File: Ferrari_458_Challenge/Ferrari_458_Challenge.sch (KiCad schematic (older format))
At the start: 16 parts, among them P1 SERVO, P2 ESC, P3 LEFT_IR, P4 RIGHT_IR, P5 ULTRASONIC, U1 LM7805, U2 FS-R6B

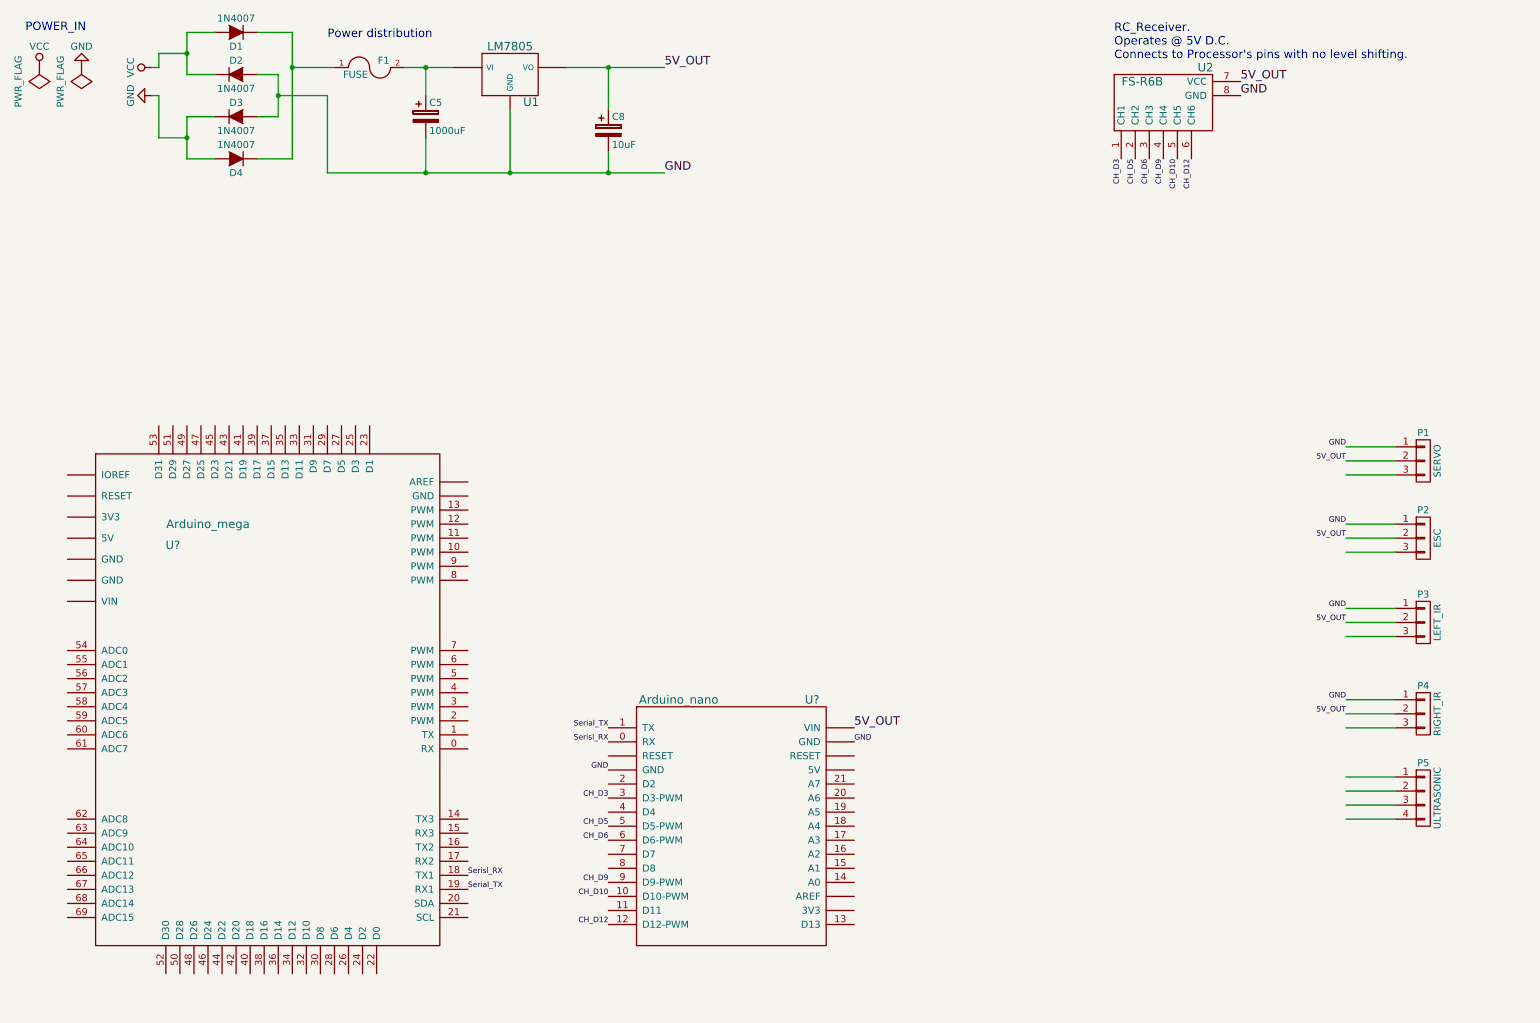
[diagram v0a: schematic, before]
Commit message: Pin Assignment
Added the voltage dividers for voltage measurements across available
batteries.
assigned some sensors to Arduino pins.
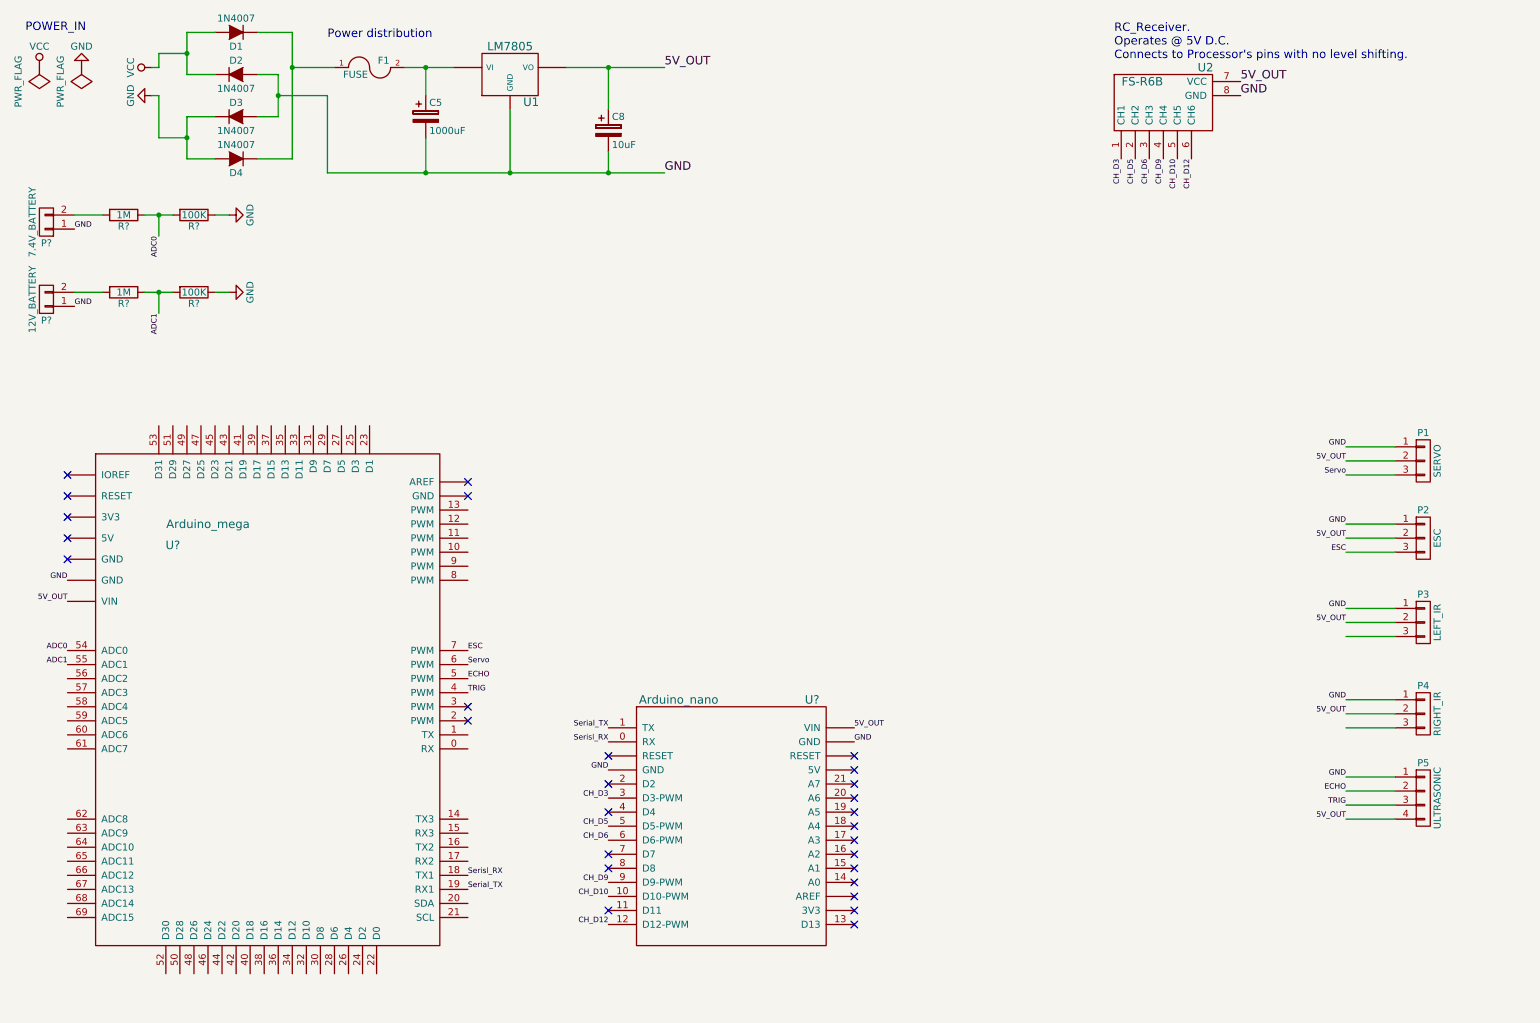
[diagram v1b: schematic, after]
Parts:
- added P?: 7.4V_BATTERY, symbol CONN_01X02
- added P?: 12V_BATTERY, symbol CONN_01X02
- added R? (x2): 1M, symbol R
- added R? (x2): 100K, symbol R
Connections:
- net labels added: ADC0, ADC1, ECHO, ESC, Servo, TRIG
- wire segments 54 -> 53
- no-connect marks 0 -> 28
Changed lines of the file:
@@
 	4800 1650 4800 1500
 Wire Wire Line
-	4500 900  4800 900
-Wire Wire Line
-	4800 900  5200 900
+	4500 900  5200 900
 Wire Wire Line
 	4800 900  4800 1200
@@
 Connection ~ 4800 1650
 Wire Wire Line
-	3350 900  3500 900
-Wire Wire Line
-	3500 900  3700 900
+	3350 900  3700 900
 Wire Wire Line
 	3500 1100 3500 900
@@
 	2450 1250 2300 1250
 Wire Wire Line
-	2450 950  2450 1100
-Wire Wire Line
-	2450 1100 2450 1250
+	2450 950  2450 1250
 Wire Wire Line
 	2450 950  2300 950
@@
 	2550 1550 2300 1550
 Wire Wire Line
-	2550 650  2550 900
-Wire Wire Line
-	2550 900  2550 1550
+	2550 650  2550 1550
 Wire Wire Line
 	2550 650  2300 650
@@
 	1800 1550 2000 1550
 Wire Wire Line
-	1800 1250 1800 1400
-Wire Wire Line
-	1800 1400 1800 1550
+	1800 1250 1800 1550
 Wire Wire Line
 	1800 1250 2000 1250
@@
 	1800 950  2000 950
 Wire Wire Line
-	1800 650  1800 800
-Wire Wire Line
-	1800 800  1800 950
+	1800 650  1800 950
 Wire Wire Line
 	1800 650  2000 650
@@
 	2800 1100 2800 1650
 Wire Wire Line
-	2800 1650 3500 1650
-Wire Wire Line
-	3500 1650 4100 1650
-Wire Wire Line
-	4100 1650 4800 1650
-Wire Wire Line
-	4800 1650 5200 1650
+	2800 1650 5200 1650
 Wire Wire Line
 	2850 900  2550 900
@@
 	1    0    0    -1
 $EndComp
-Text Label 6550 5600 0    60   ~ 0
+Text Label 6550 5600 0    39   ~ 0
 5V_OUT
 Text Label 6550 5700 0    39   ~ 0
@@
 Text Label 4800 5700 2    39   ~ 0
 Serisl_RX
+NoConn ~ 3800 5550
+NoConn ~ 3800 5450
+NoConn ~ 4800 5800
+NoConn ~ 6550 5800
+NoConn ~ 6550 5900
+NoConn ~ 4800 6000
+NoConn ~ 4800 6200
+NoConn ~ 4800 6500
+NoConn ~ 4800 6600
+NoConn ~ 4800 6900
+NoConn ~ 6550 6000
+NoConn ~ 6550 6100
+NoConn ~ 6550 6200
+NoConn ~ 6550 6300
+NoConn ~ 6550 6400
+NoConn ~ 6550 6500
+NoConn ~ 6550 6600
+NoConn ~ 6550 6700
+NoConn ~ 6550 6800
+NoConn ~ 6550 6900
+NoConn ~ 6550 7000
+Text Label 3800 5150 0    39   ~ 0
+Servo
+Text Label 3800 5050 0    39   ~ 0
+ESC
+Text Label 10050 3800 2    39   ~ 0
+Servo
+Text Label 10050 4350 2    39   ~ 0
+ESC
+Text Label 3800 5250 0    39   ~ 0
+ECHO
+Text Label 3800 5350 0    39   ~ 0
+TRIG
+Text Label 10050 5950 2    39   ~ 0
+GND
+Text Label 10050 6050 2    39   ~ 0
+ECHO
+Text Label 10050 6150 2    39   ~ 0
+TRIG
+Text Label 10050 6250 2    39   ~ 0
+5V_OUT
+Text Label 950  4700 2    39   ~ 0
+5V_OUT
+Text Label 950  4550 2    39   ~ 0
+GND
+NoConn ~ 950  4400
+NoConn ~ 950  4250
+NoConn ~ 950  4100
+NoConn ~ 950  3950
+NoConn ~ 950  3800
+NoConn ~ 3800 3850
+NoConn ~ 3800 3950
+$Comp
+L R R?
+U 1 1 57168707
+P 1350 1950
+F 0 "R?" V 1430 1950 50  0000 C CNN
+F 1 "1M" V 1350 1950 50  0000 C CNN
+F 2 "" V 1280 1950 50  0000 C CNN
+F 3 "" H 1350 1950 50  0000 C CNN
+	1    1350 1950
+	0    1    1    0
+$EndComp
+$Comp
+L R R?
+U 1 1 57168768
+P 1850 1950
+F 0 "R?" V 1930 1950 50  0000 C CNN
+F 1 "100K" V 1850 1950 50  0000 C CNN
+F 2 "" V 1780 1950 50  0000 C CNN
+F 3 "" H 1850 1950 50  0000 C CNN
+	1    1850 1950
+	0    1    1    0
+$EndComp
+Wire Wire Line
+	1500 1950 1700 1950
+$Comp
+L GND #PWR?
+U 1 1 571687FA
+P 2100 1950
+F 0 "#PWR?" H 2100 1700 50  0001 C CNN
+F 1 "GND" H 2100 1800 50  0000 C CNN
+F 2 "" H 2100 1950 50  0000 C CNN
+F 3 "" H 2100 1950 50  0000 C CNN
+	1    2100 1950
+	0    -1   -1   0
+$EndComp
+Wire Wire Line
+	2100 1950 2000 1950
+Connection ~ 1600 1950
+Wire Wire Line
+	1600 1950 1600 2100
+Text Label 1600 2100 3    39   ~ 0
+ADC0
+$Comp
+L CONN_01X02 P?
+U 1 1 57168C66
+P 800 2000
+F 0 "P?" H 800 2150 50  0000 C CNN
+F 1 "7.4V_BATTERY" V 900 2000 50  0000 C CNN
+F 2 "" H 800 2000 50  0000 C CNN
+F 3 "" H 800 2000 50  0000 C CNN
+	1    800  2000
+	-1   0    0    1
+$EndComp
+Wire Wire Line
+	1000 1950 1200 1950
+Text Label 1000 2050 0    39   ~ 0
+GND
+$Comp
+L R R?
+U 1 1 57169476
+P 1350 2500
+F 0 "R?" V 1430 2500 50  0000 C CNN
+F 1 "1M" V 1350 2500 50  0000 C CNN
+F 2 "" V 1280 2500 50  0000 C CNN
+F 3 "" H 1350 2500 50  0000 C CNN
+	1    1350 2500
+	0    1    1    0
+$EndComp
+$Comp
+L R R?
+U 1 1 5716947C
+P 1850 2500
+F 0 "R?" V 1930 2500 50  0000 C CNN
+F 1 "100K" V 1850 2500 50  0000 C CNN
+F 2 "" V 1780 2500 50  0000 C CNN
+F 3 "" H 1850 2500 50  0000 C CNN
+	1    1850 2500
+	0    1    1    0
+$EndComp
+Wire Wire Line
+	1500 2500 1700 2500
+$Comp
+L GND #PWR?
+U 1 1 57169483
+P 2100 2500
+F 0 "#PWR?" H 2100 2250 50  0001 C CNN
+F 1 "GND" H 2100 2350 50  0000 C CNN
+F 2 "" H 2100 2500 50  0000 C CNN
+F 3 "" H 2100 2500 50  0000 C CNN
+	1    2100 2500
+	0    -1   -1   0
+$EndComp
+Wire Wire Line
+	2100 2500 2000 2500
+Connection ~ 1600 2500
+Wire Wire Line
+	1600 2500 1600 2650
+Text Label 1600 2650 3    39   ~ 0
+ADC1
+$Comp
+L CONN_01X02 P?
+U 1 1 5716948D
+P 800 2550
+F 0 "P?" H 800 2700 50  0000 C CNN
+F 1 "12V_BATTERY" V 900 2550 50  0000 C CNN
+F 2 "" H 800 2550 50  0000 C CNN
+F 3 "" H 800 2550 50  0000 C CNN
+	1    800  2550
+	-1   0    0    1
+$EndComp
+Wire Wire Line
+	1000 2500 1200 2500
+Text Label 1000 2600 0    39   ~ 0
+GND
+Text Label 950  5050 2    39   ~ 0
+ADC0
+Text Label 950  5150 2    39   ~ 0
+ADC1
 $EndSCHEMATC

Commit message: A new method to read the signals from receiver
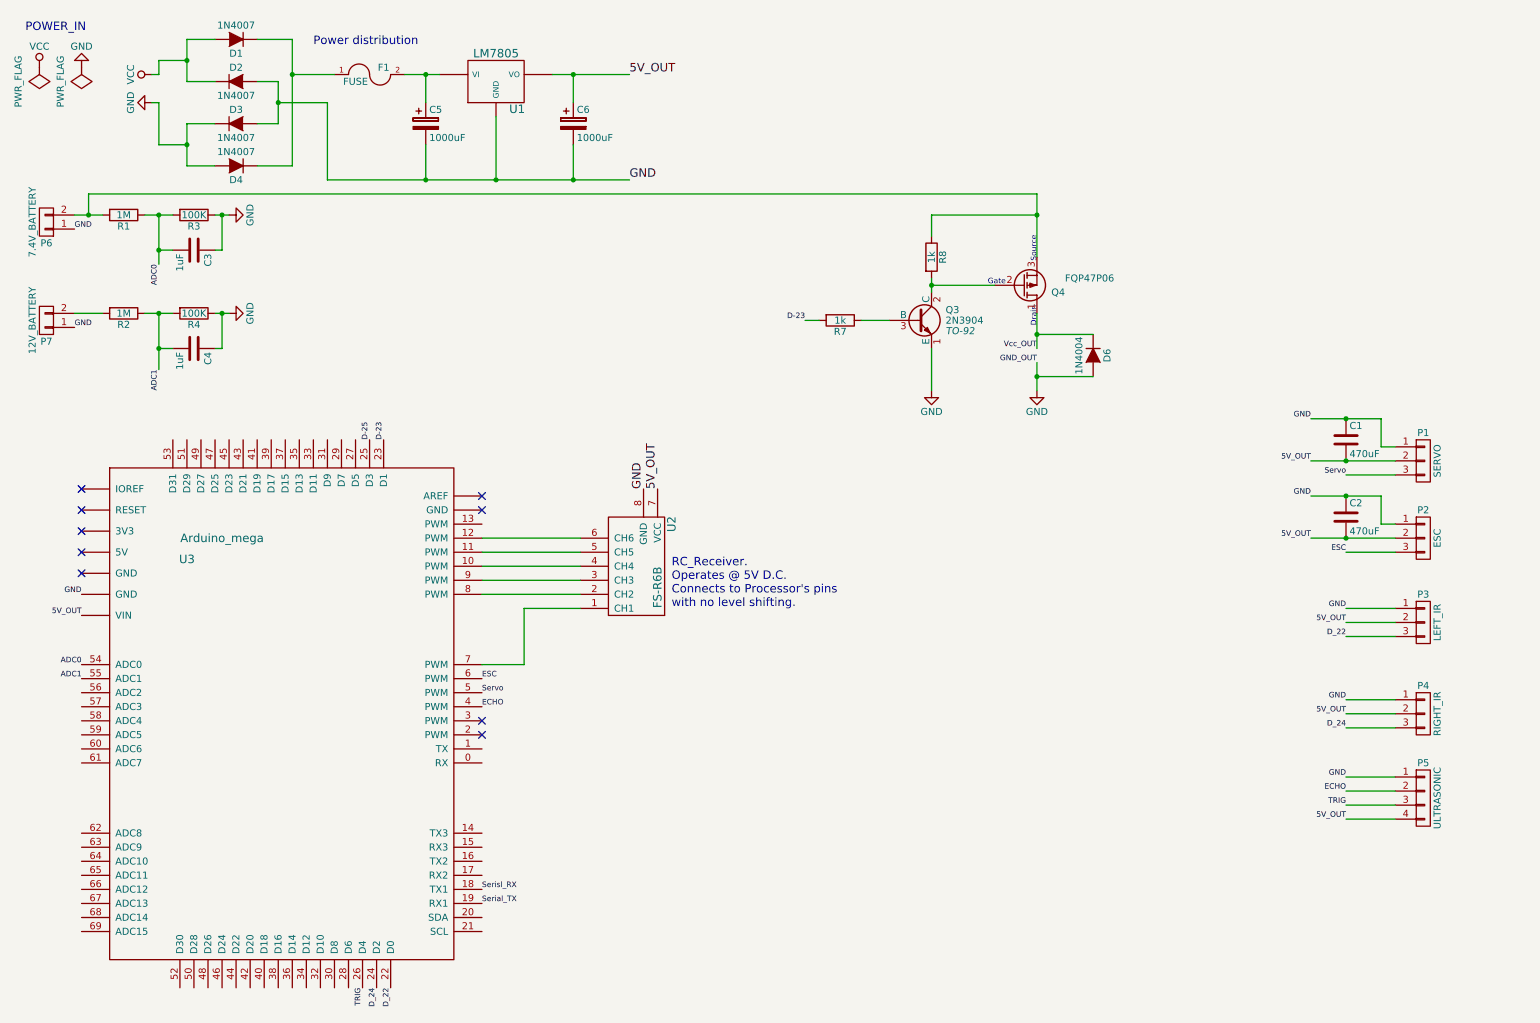
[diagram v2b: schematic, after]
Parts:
- removed C8: 10uF, Capacitors_ThroughHole:C_Radial_D5_L11_P2, symbol CP
- removed U?: Arduino_nano, symbol Arduino_nano
- added C1, C2: 470uF, symbol C
- added C3, C4: 1uF, symbol C
- added C6: 1000uF, Capacitors_ThroughHole:C_Radial_D5_L6_P2.5, symbol CP
- added D6: 1N4004, symbol D
- added Q3: 2N3904, TO-92, symbol 2SC1815
- added Q4: FQP47P06, symbol Q_PMOS_DGS
- added R7, R8: 1k, symbol R
- gave numbers to parts that had none: 7
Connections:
- net labels added: D-23, D-25, D_22, D_24, GND_OUT, Vcc_OUT
- net labels removed: CH_D10, CH_D12, CH_D3, CH_D5, CH_D6, CH_D9
- wire segments 53 -> 85
- no-connect marks 28 -> 9
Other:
- note added: "Drain"
- note added: "Gate"
- note added: "RC_Receiver. \nOperates @ 5V D.C. \nConnects to Processor's pins\nwith no level shifting."
- note added: "Source"
- note removed: "RC_Receiver. \nOperates @ 5V D.C. \nConnects to Processor's pins with no level shifting."
- moved on the sheet: C5, D1, D2, D3, D4, F1, P7, R2, R4, U1, U2, U3

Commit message: Schematic update
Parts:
- removed C2: 470uF, symbol C
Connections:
- net 5V_OUT: no longer P2.2 (P2)
- net at U2.1 (CH1): now also U3.62 (ADC8); no longer U3.7 (PWM)
- net at U2.2 (CH2): now also U3.63 (ADC9); no longer U3.8 (PWM)
- net at U2.3 (CH3): now also U3.64 (ADC10); no longer U3.9 (PWM)
- net at U2.4 (CH4): now also U3.65 (ADC11); no longer U3.10 (PWM)
- net at U2.5 (CH5): now also U3.66 (ADC12); no longer U3.11 (PWM)
- net at U2.6 (CH6): now also U3.67 (ADC13); no longer U3.12 (PWM)
- net D-25: no longer names the net of U3.25 (D3)
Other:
- moved on the sheet: C1, C3, D6, P1, P2, P3, P4, P5, P6, Q3, Q4, R1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
